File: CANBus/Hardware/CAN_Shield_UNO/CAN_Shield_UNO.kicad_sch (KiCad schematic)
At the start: 9 parts, among them J1 Power, J2 Digital/PWM, J3 Analog, J4 Digital/PWM, J6 Screw_Terminal_01x02, U2 TCAN1051HGV

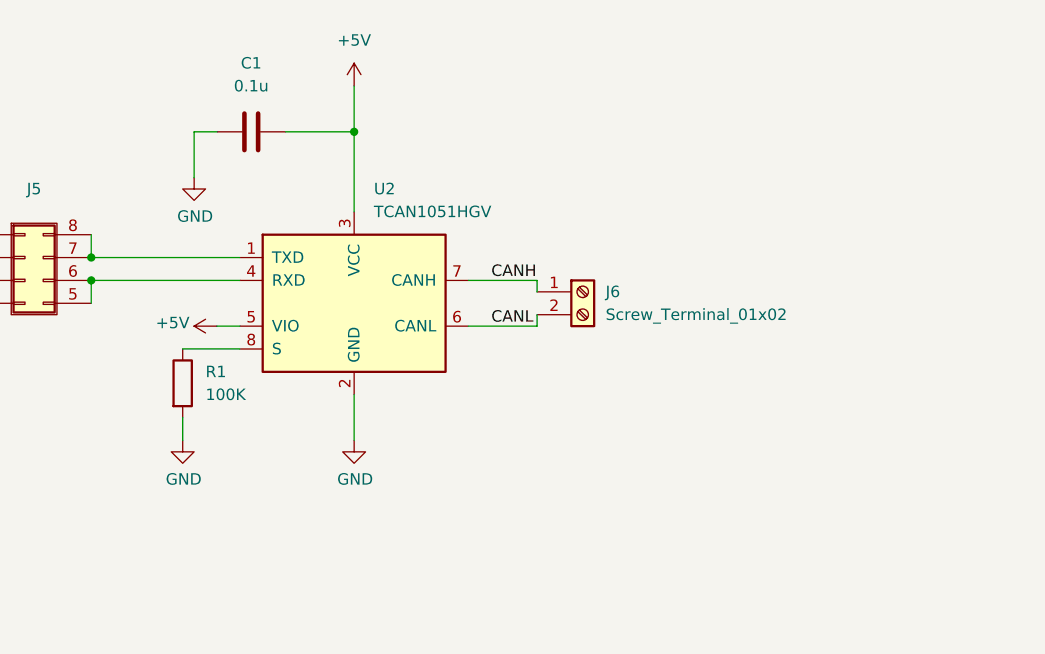
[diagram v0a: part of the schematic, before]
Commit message: feat: added  termination resistors and sent pin S to digital pin 2
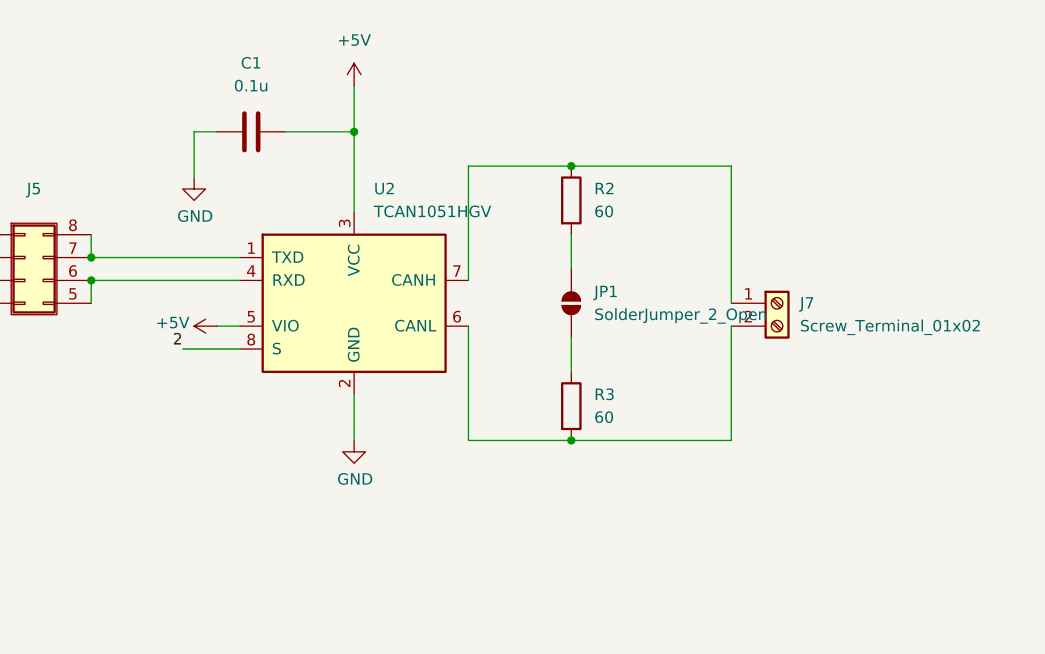
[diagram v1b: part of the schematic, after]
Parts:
- removed J6: Screw_Terminal_01x02, symbol Connector:Screw_Terminal_01x02
- removed R1: 100K, symbol Device:R
- added J7: Screw_Terminal_01x02, symbol Connector:Screw_Terminal_01x02
- added JP1: SolderJumper_2_Open, symbol Jumper:SolderJumper_2_Open
- added R2, R3: 60, symbol Device:R
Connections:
- net 2: now also U2.8 (S)
- net CANH: no longer names the net of U2.7 (CANH)
- net CANH: now also J7.1 (Pin_1), R2.1
- net CANL: no longer names the net of U2.6 (CANL)
- net CANL: now also J7.2 (Pin_2), R3.2
- new net: JP1.1 (A), R3.1
- new net: JP1.2 (B), R2.2

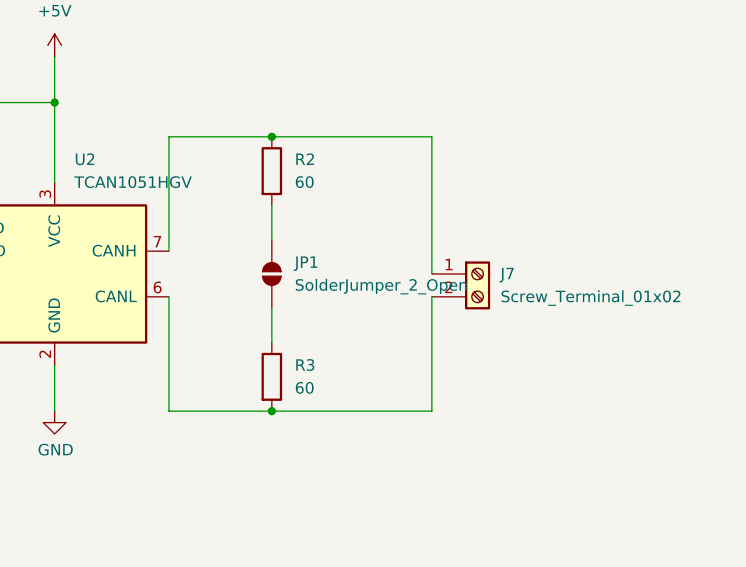
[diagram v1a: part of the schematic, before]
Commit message: fix: change to bridged solder jumper and remove backup files
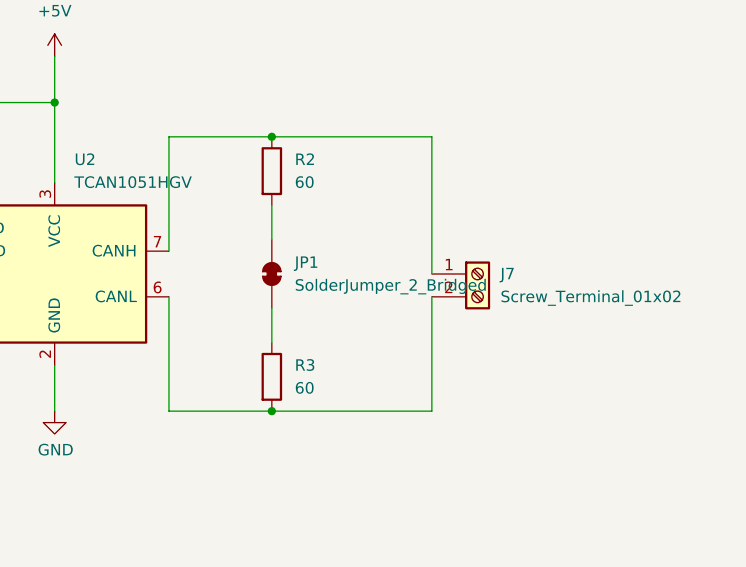
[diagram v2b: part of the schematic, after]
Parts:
- removed JP1: SolderJumper_2_Open, symbol Jumper:SolderJumper_2_Open
- added JP1: SolderJumper_2_Bridged, symbol Jumper:SolderJumper_2_Bridged
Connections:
- net at R3.1: now also JP1.1 (A)
- net at R2.2: now also JP1.2 (B)
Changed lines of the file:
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@@
+	)
+	(symbol
+		(lib_id "Jumper:SolderJumper_2_Bridged")
+		(at 167.64 50.8 90)
+		(unit 1)
+		(exclude_from_sim yes)
+		(in_bom no)
+		(on_board yes)
+		(dnp no)
+		(fields_autoplaced yes)
+		(property "Reference" "JP1"
+			(at 170.18 49.5299 90)
+			(effects
+				(font
+					(size 1.27 1.27)
+				)
+				(justify right)
+			)
+		)
+		(property "Value" "SolderJumper_2_Bridged"
+			(at 170.18 52.0699 90)
+			(effects
+				(font
+					(size 1.27 1.27)
+				)
+				(justify right)
+			)
+		)
+		(property "Footprint" ""
+			(at 167.64 50.8 0)
+			(effects
+				(font
+					(size 1.27 1.27)
+				)
+				(hide yes)
+			)
+		)
+		(property "Datasheet" "~"
+			(at 167.64 50.8 0)
+			(effects
+				(font
+					(size 1.27 1.27)
+				)
+				(hide yes)
+			)
+		)
+		(property "Description" "Solder Jumper, 2-pole, closed/bridged"
+			(at 167.64 50.8 0)
+			(effects
+				(font
+					(size 1.27 1.27)
+				)
+				(hide yes)
+			)
+		)
+		(pin "1"
+		)
+		(pin "2"
+		)
+		(instances
+			(project "CAN_Shield_UNO"
+				(path "/e63e39d7-6ac0-4ffd-8aa3-1841a4541b55"
+					(reference "JP1")
+					(unit 1)
+				)
+			)
+		)
 	)
 	(symbol
@@
 					(unit 1)
 				)
-			)
-		)
-	)
-	(symbol
-		(lib_id "Jumper:SolderJumper_2_Open")
-		(at 167.64 50.8 90)
-		(unit 1)
-		(exclude_from_sim yes)
-		(in_bom no)
-		(on_board yes)
-		(dnp no)
-		(fields_autoplaced yes)
-		(property "Reference" "JP1"
-			(at 170.18 49.5299 90)
-			(effects
-				(font
-					(size 1.27 1.27)
-				)
-				(justify right)
-			)
-		)
-		(property "Value" "SolderJumper_2_Open"
-			(at 170.18 52.0699 90)
-			(effects
-				(font
-					(size 1.27 1.27)
-				)
-				(justify right)
-			)
-		)
-		(property "Footprint" ""
-			(at 167.64 50.8 0)
-			(effects
-				(font
-					(size 1.27 1.27)
-				)
-				(hide yes)
-			)
-		)
-		(property "Datasheet" "~"
-			(at 167.64 50.8 0)
-			(effects
-				(font
-					(size 1.27 1.27)
-				)
-				(hide yes)
-			)
-		)
-		(property "Description" "Solder Jumper, 2-pole, open"
-			(at 167.64 50.8 0)
-			(effects
-				(font
-					(size 1.27 1.27)
-				)
-				(hide yes)
-			)
-		)
-		(pin "1"
-		)
-		(pin "2"
-		)
-		(instances
-			(project "CAN_Shield_UNO"
-				(path "/e63e39d7-6ac0-4ffd-8aa3-1841a4541b55"
-					(reference "JP1")
-					(unit 1)
-				)

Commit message: feat: added PCB design
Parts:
- C1: footprint (none) -> Capacitor_SMD:C_0805_2012Metric_Pad1.18x1.45mm_HandSolder; LCSC# (none) -> C38141; Proveedor (none) -> LCSC; manf# (none) -> 0805B104K500NT
- J1, J2, J3, J4: Proveedor (none) -> MOUSER/DIGIKEY; manf# (none) -> PRT-14322
- J5: footprint (none) -> Connector_PinHeader_2.54mm:PinHeader_2x04_P2.54mm_Vertical; LCSC# (none) -> C18197999; Proveedor (none) -> LCSC; manf# (none) -> PZ254-2-04-Z-2.5-G1
- J7: footprint (none) -> TerminalBlock:TerminalBlock_bornier-2_P5.08mm; Proveedor (none) -> STEREN; manf# (none) -> TRT-02
- JP1: footprint (none) -> Connector_PinHeader_2.54mm:PinHeader_1x02_P2.54mm_Vertical; LCSC# (none) -> C492401; Proveedor (none) -> LCSC; manf# (none) -> PZ254V-11-02P
- R2, R3: footprint (none) -> Resistor_SMD:R_0201_0603Metric; LCSC# (none) -> C166918; Proveedor (none) -> LCSC; manf# (none) -> RTT0360R0FTP
- U2: footprint (none) -> Package_SO:SOIC-8_3.9x4.9mm_P1.27mm; LCSC# (none) -> C424093; Proveedor (none) -> LCSC; manf# (none) -> MCP73831T-2ACI/OT

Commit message: feat: Resistors got changed
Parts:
- C1: manf# 0805B104K500NT -> 0805B104K500NT
- R2, R3: footprint Resistor_SMD:R_0201_0603Metric -> Resistor_SMD:R_1206_3216Metric_Pad1.30x1.75mm_HandSolder; LCSC# C166918 -> (none); Proveedor LCSC -> MOUSER; manf# RTT0360R0FTP -> 71-CRCW120660R0KNAIF
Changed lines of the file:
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@@
 			)
 		)
-		(property "Footprint" "Resistor_SMD:R_0201_0603Metric"
+		(property "Footprint" "Resistor_SMD:R_1206_3216Metric_Pad1.30x1.75mm_HandSolder"
 			(at 165.862 62.23 90)
 			(effects
@@
 			)
 		)
-		(property "LCSC#" "C166918"
+		(property "LCSC#" ""
 			(at 167.64 62.23 0)
 			(effects
@@
 			)
 		)
-		(property "Proveedor" "LCSC"
+		(property "Proveedor" "MOUSER"
 			(at 167.64 62.23 0)
 			(effects
@@
 			)
 		)
-		(property "manf#" "RTT0360R0FTP"
+		(property "manf#" "71-CRCW120660R0KNAIF"
 			(at 167.64 62.23 0)
 			(effects
@@
 			)
 		)
-		(property "manf#" "0805B104K500NT"
+		(property "manf#" " 0805B104K500NT"
 			(at 132.08 31.75 0)
 			(effects
@@
 			)
 		)
-		(property "Footprint" "Resistor_SMD:R_0201_0603Metric"
+		(property "Footprint" "Resistor_SMD:R_1206_3216Metric_Pad1.30x1.75mm_HandSolder"
 			(at 165.862 39.37 90)
 			(effects
@@
 			)
 		)
-		(property "LCSC#" "C166918"
+		(property "LCSC#" ""
 			(at 167.64 39.37 0)
 			(effects
@@
 			)
 		)
-		(property "Proveedor" "LCSC"
+		(property "Proveedor" "MOUSER"
 			(at 167.64 39.37 0)
 			(effects
@@
 			)
 		)
-		(property "manf#" "RTT0360R0FTP"
+		(property "manf#" "71-CRCW120660R0KNAIF"
 			(at 167.64 39.37 0)
 			(effects

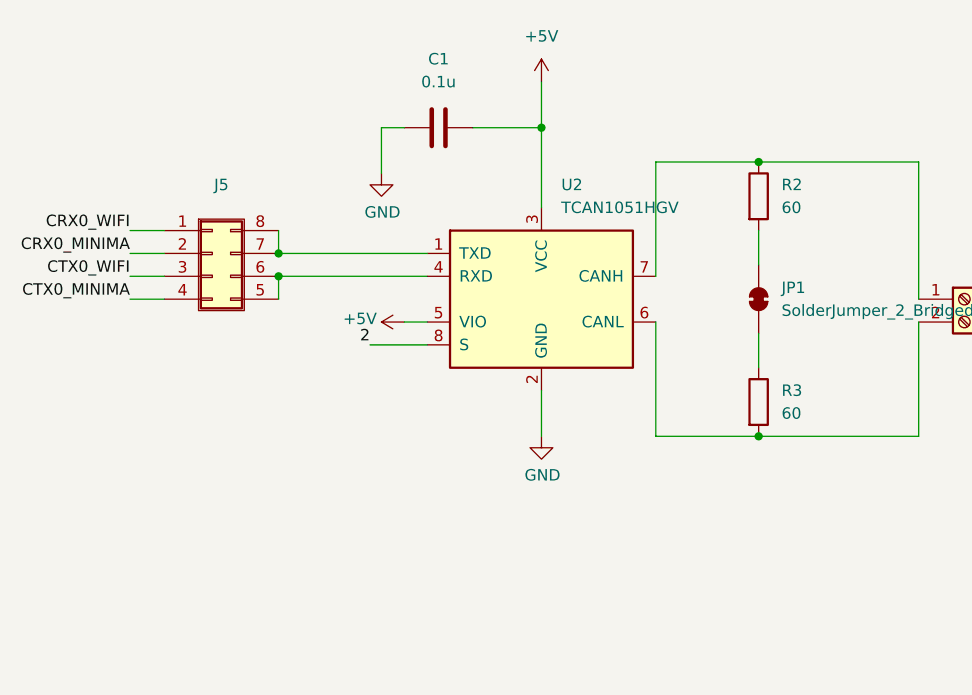
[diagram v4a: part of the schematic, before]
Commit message: feat(Hw): Route PCB
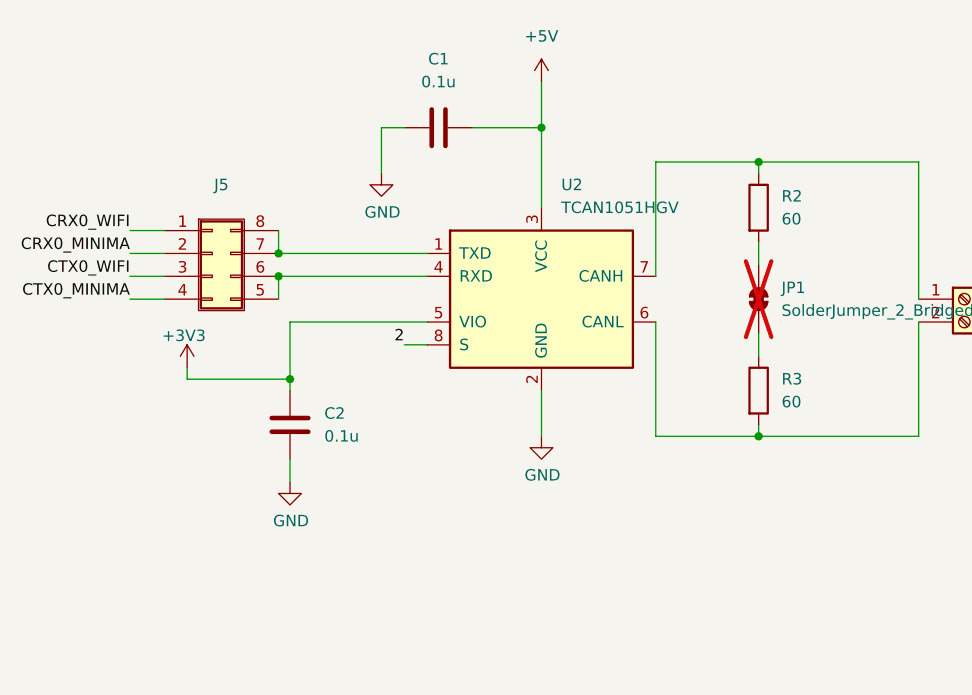
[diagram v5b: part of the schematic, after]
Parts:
- added C2: 0.1u, Capacitor_SMD:C_0805_2012Metric_Pad1.18x1.45mm_HandSolder, symbol Device:C
- JP1: footprint Connector_PinHeader_2.54mm:PinHeader_1x02_P2.54mm_Vertical -> Jumper:SolderJumper-2_P1.3mm_Bridged_Pad1.0x1.5mm; LCSC# C492401 -> (none); Proveedor LCSC -> (none); manf# PZ254V-11-02P -> (none); now not fitted
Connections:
- net +3V3: now also U2.5 (VIO), C2.1
- net +5V: no longer U2.5 (VIO)
- net GND: now also C2.2
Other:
- moved on the sheet: R2, R3

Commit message: feat(hw): Bom updated
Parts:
- C1: manf# 0805B104K500NT -> 0805B104K500NT
- U2: LCSC# C424093 -> (none); Proveedor LCSC -> MOUSER; manf# MCP73831T-2ACI/OT -> 595-TCAN1051HGVDR
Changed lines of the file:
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@@
 			)
 		)
-		(property "manf#" " 0805B104K500NT"
+		(property "manf#" "0805B104K500NT"
 			(at 132.08 31.75 0)
 			(effects
@@
 			)
 		)
-		(property "LCSC#" "C424093"
-			(at 143.51 50.8 0)
-			(effects
-				(font
-					(size 1.27 1.27)
-				)
-				(hide yes)
-			)
-		)
-		(property "Proveedor" "LCSC"
-			(at 143.51 50.8 0)
-			(effects
-				(font
-					(size 1.27 1.27)
-				)
-				(hide yes)
-			)
-		)
-		(property "manf#" "MCP73831T-2ACI/OT"
-			(at 143.51 50.8 0)
-			(effects
+		(property "LCSC#" ""
+			(at 143.51 50.8 0)
+			(effects
+				(font
+					(size 1.27 1.27)
+				)
+				(hide yes)
+			)
+		)
+		(property "Proveedor" "MOUSER"
+			(at 143.51 50.8 0)
+			(effects
+				(font
+					(size 1.27 1.27)
+				)
+				(hide yes)
+			)
+		)
+		(property "manf#" "595-TCAN1051HGVDR"
+			(at 143.51 50.8 0)
+			(effects

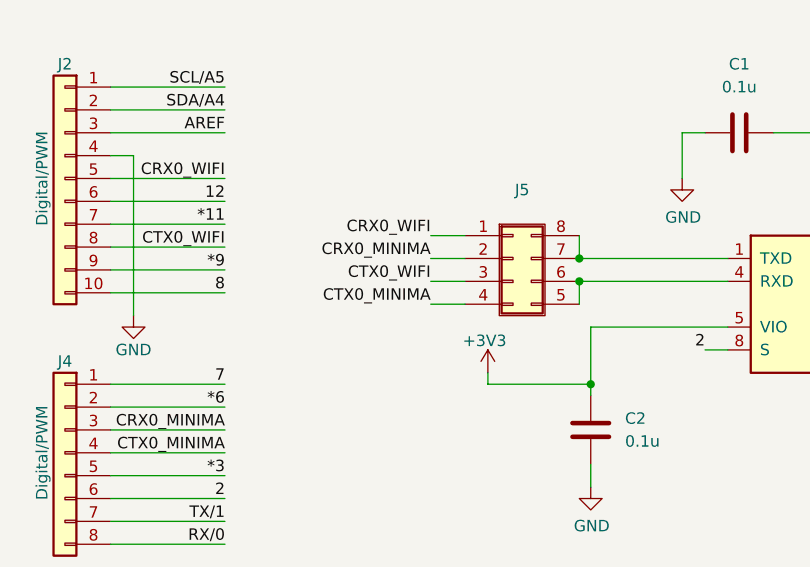
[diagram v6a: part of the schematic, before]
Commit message: fix: change RX  and TX position
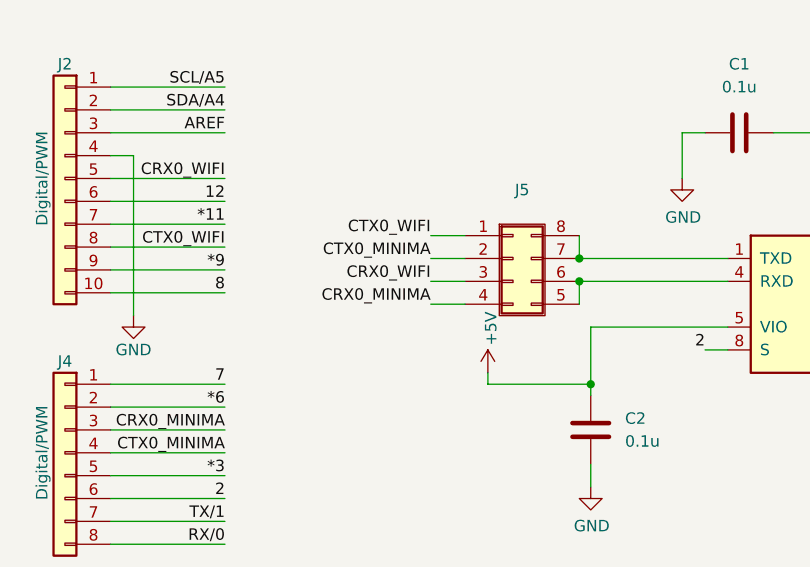
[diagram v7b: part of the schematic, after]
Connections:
- net +3V3: no longer C2.1, U2.5 (VIO)
- net +5V: now also C2.1, U2.5 (VIO)
- net CRX0_MINIMA: now also J5.4 (Pin_4); no longer J5.2 (Pin_2)
- net CRX0_WIFI: now also J5.3 (Pin_3); no longer J5.1 (Pin_1)
- net CTX0_MINIMA: now also J5.2 (Pin_2); no longer J5.4 (Pin_4)
- net CTX0_WIFI: now also J5.1 (Pin_1); no longer J5.3 (Pin_3)
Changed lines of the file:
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@@
 	)
 	(label "CRX0_MINIMA"
-		(at 97.79 45.72 180)
+		(at 97.79 50.8 180)
 		(fields_autoplaced yes)
 		(effects
@@
 	)
 	(label "CTX0_MINIMA"
-		(at 97.79 50.8 180)
+		(at 97.79 45.72 180)
 		(fields_autoplaced yes)
 		(effects
@@
 	)
 	(label "CTX0_WIFI"
-		(at 97.79 48.26 180)
+		(at 97.79 43.18 180)
 		(fields_autoplaced yes)
 		(effects
@@
 	)
 	(label "CRX0_WIFI"
-		(at 97.79 43.18 180)
+		(at 97.79 48.26 180)
 		(fields_autoplaced yes)
 		(effects
@@
 	)
 	(symbol
+		(lib_id "power:+5V")
+		(at 104.14 58.42 0)
+		(unit 1)
+		(exclude_from_sim no)
+		(in_bom yes)
+		(on_board yes)
+		(dnp no)
+		(property "Reference" "#PWR06"
+			(at 104.14 62.23 0)
+			(effects
+				(font
+					(size 1.27 1.27)
+				)
+				(hide yes)
+			)
+		)
+		(property "Value" "+5V"
+			(at 104.4956 55.372 90)
+			(effects
+				(font
+					(size 1.27 1.27)
+				)
+				(justify left)
+			)
+		)
+		(property "Footprint" ""
+			(at 104.14 58.42 0)
+			(effects
+				(font
+					(size 1.27 1.27)
+				)
+			)
+		)
+		(property "Datasheet" ""
+			(at 104.14 58.42 0)
+			(effects
+				(font
+					(size 1.27 1.27)
+				)
+			)
+		)
+		(property "Description" ""
+			(at 104.14 58.42 0)
+			(effects
+				(font
+					(size 1.27 1.27)
+				)
+				(hide yes)
+			)
+		)
+		(pin "1"
+		)
+		(instances
+			(project "CAN_Shield_UNO"
+				(path "/e63e39d7-6ac0-4ffd-8aa3-1841a4541b55"
+					(reference "#PWR06")
+					(unit 1)
+				)
+			)
+		)
+	)
+	(symbol
 		(lib_id "Device:R")
 		(at 167.64 60.96 0)
@@
 					(unit 1)
 				)
-			)
-		)
-	)
-	(symbol
-		(lib_id "power:+3.3V")
-		(at 104.14 58.42 0)
-		(unit 1)
-		(exclude_from_sim no)
-		(in_bom yes)
-		(on_board yes)
-		(dnp no)
-		(property "Reference" "#PWR06"
-			(at 104.14 62.23 0)
-			(effects
-				(font
-					(size 1.27 1.27)
-				)
-				(hide yes)
-			)
-		)
-		(property "Value" "+3V3"
-			(at 101.346 54.864 0)
-			(effects
-				(font
-					(size 1.27 1.27)
-				)
-				(justify left)
-			)
-		)
-		(property "Footprint" ""
-			(at 104.14 58.42 0)
-			(effects
-				(font
-					(size 1.27 1.27)
-				)
-				(hide yes)
-			)
-		)
-		(property "Datasheet" ""
-			(at 104.14 58.42 0)
-			(effects
-				(font
-					(size 1.27 1.27)
-				)
-				(hide yes)
-			)
-		)
-		(property "Description" "Power symbol creates a global label with name \"+3.3V\""
-			(at 104.14 58.42 0)
-			(effects
-				(font
-					(size 1.27 1.27)
-				)
-				(hide yes)
-			)
-		)
-		(pin "1"
-		)
-		(instances
-			(project "CAN_Shield_UNO"
-				(path "/e63e39d7-6ac0-4ffd-8aa3-1841a4541b55"
-					(reference "#PWR06")
-					(unit 1)
-				)
